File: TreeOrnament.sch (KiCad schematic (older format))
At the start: 13 parts, among them J1 USB_B_Micro

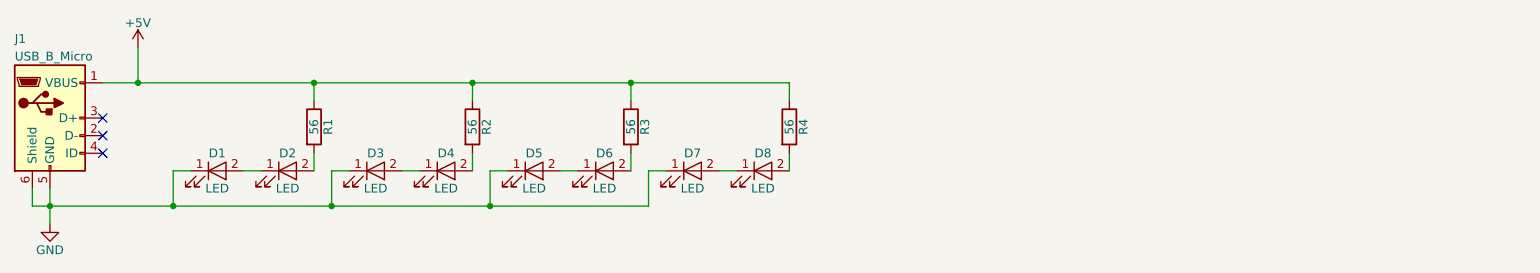
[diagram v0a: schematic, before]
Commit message: add more LEDs to schematic
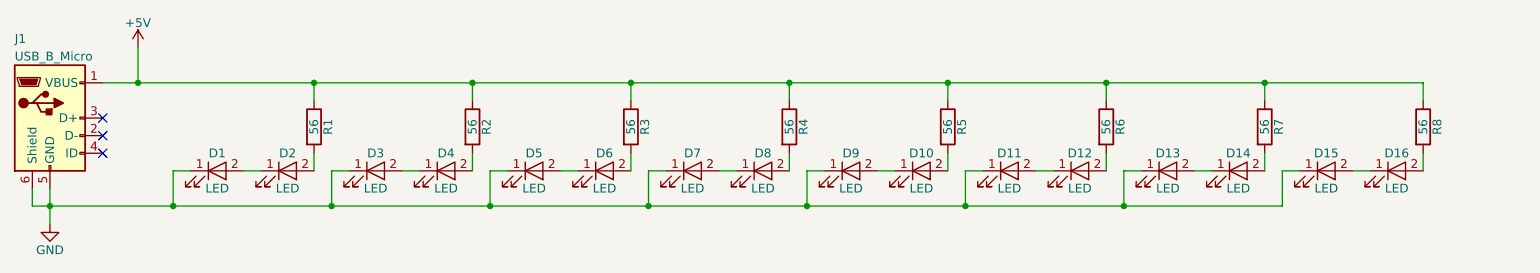
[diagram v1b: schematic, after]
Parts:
- added D10, D11, D12, D13, D14, D15, D16, D9: LED, LEDs:LED_D3.0mm, symbol LED
- added R5, R6, R7, R8: 56, Resistors_THT:R_Axial_DIN0207_L6.3mm_D2.5mm_P7.62mm_Horizontal, symbol R
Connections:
- net +5V: now also R5.1, R6.1, R7.1, R8.1
- net GND: now also D11.1 (K), D13.1 (K), D15.1 (K), D9.1 (K)
- new net: D10.1 (K), D9.2 (A)
- new net: D10.2 (A), R5.2
- new net: D11.2 (A), D12.1 (K)
- new net: D12.2 (A), R6.2
- new net: D13.2 (A), D14.1 (K)
- new net: D14.2 (A), R7.2
- new net: D15.2 (A), D16.1 (K)
- new net: D16.2 (A), R8.2
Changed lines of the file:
@@
 $EndComp
 Wire Wire Line
-	1800 1200 5700 1200
+	1800 1200 9300 1200
 Wire Wire Line
 	2000 1200 2000 1000
@@
 	1400 1800 1400 1900
 Wire Wire Line
-	1400 1900 4900 1900
+	1400 1900 8500 1900
 Connection ~ 1500 1900
 $Comp
@@
 NoConn ~ 1800 1500
 NoConn ~ 1800 1600
+$Comp
+L LED D9
+U 1 1 59F0E50C
+P 6050 1700
+F 0 "D9" H 6050 1800 50  0000 C CNN
+F 1 "LED" H 6050 1600 50  0000 C CNN
+F 2 "LEDs:LED_D3.0mm" H 6050 1700 50  0001 C CNN
+F 3 "" H 6050 1700 50  0001 C CNN
+	1    6050 1700
+	1    0    0    -1
+$EndComp
+$Comp
+L LED D10
+U 1 1 59F0ED31
+P 6450 1700
+F 0 "D10" H 6450 1800 50  0000 C CNN
+F 1 "LED" H 6450 1600 50  0000 C CNN
+F 2 "LEDs:LED_D3.0mm" H 6450 1700 50  0001 C CNN
+F 3 "" H 6450 1700 50  0001 C CNN
+	1    6450 1700
+	1    0    0    -1
+$EndComp
+$Comp
+L R R5
+U 1 1 59F0ED78
+P 6600 1450
+F 0 "R5" V 6680 1450 50  0000 C CNN
+F 1 "56" V 6600 1450 50  0000 C CNN
+F 2 "Resistors_THT:R_Axial_DIN0207_L6.3mm_D2.5mm_P7.62mm_Horizontal" V 6530 1450 50  0001 C CNN
+F 3 "" H 6600 1450 50  0001 C CNN
+	1    6600 1450
+	1    0    0    -1
+$EndComp
+Wire Wire Line
+	6600 1200 6600 1300
+Connection ~ 5700 1200
+Wire Wire Line
+	6600 1600 6600 1700
+Wire Wire Line
+	6300 1700 6200 1700
+Wire Wire Line
+	5900 1700 5800 1700
+Wire Wire Line
+	5800 1700 5800 1900
+Connection ~ 4900 1900
+$Comp
+L LED D11
+U 1 1 59F0EEA1
+P 6950 1700
+F 0 "D11" H 6950 1800 50  0000 C CNN
+F 1 "LED" H 6950 1600 50  0000 C CNN
+F 2 "LEDs:LED_D3.0mm" H 6950 1700 50  0001 C CNN
+F 3 "" H 6950 1700 50  0001 C CNN
+	1    6950 1700
+	1    0    0    -1
+$EndComp
+$Comp
+L LED D12
+U 1 1 59F0EEEE
+P 7350 1700
+F 0 "D12" H 7350 1800 50  0000 C CNN
+F 1 "LED" H 7350 1600 50  0000 C CNN
+F 2 "LEDs:LED_D3.0mm" H 7350 1700 50  0001 C CNN
+F 3 "" H 7350 1700 50  0001 C CNN
+	1    7350 1700
+	1    0    0    -1
+$EndComp
+$Comp
+L R R6
+U 1 1 59F0EF38
+P 7500 1450
+F 0 "R6" V 7580 1450 50  0000 C CNN
+F 1 "56" V 7500 1450 50  0000 C CNN
+F 2 "Resistors_THT:R_Axial_DIN0207_L6.3mm_D2.5mm_P7.62mm_Horizontal" V 7430 1450 50  0001 C CNN
+F 3 "" H 7500 1450 50  0001 C CNN
+	1    7500 1450
+	1    0    0    -1
+$EndComp
+Wire Wire Line
+	7500 1200 7500 1300
+Connection ~ 6600 1200
+Wire Wire Line
+	7500 1600 7500 1700
+Wire Wire Line
+	7200 1700 7100 1700
+Wire Wire Line
+	6800 1700 6700 1700
+Wire Wire Line
+	6700 1700 6700 1900
+Connection ~ 5800 1900
+$Comp
+L LED D13
+U 1 1 59F0F258
+P 7850 1700
+F 0 "D13" H 7850 1800 50  0000 C CNN
+F 1 "LED" H 7850 1600 50  0000 C CNN
+F 2 "LEDs:LED_D3.0mm" H 7850 1700 50  0001 C CNN
+F 3 "" H 7850 1700 50  0001 C CNN
+	1    7850 1700
+	1    0    0    -1
+$EndComp
+$Comp
+L LED D14
+U 1 1 59F0F2A9
+P 8250 1700
+F 0 "D14" H 8250 1800 50  0000 C CNN
+F 1 "LED" H 8250 1600 50  0000 C CNN
+F 2 "LEDs:LED_D3.0mm" H 8250 1700 50  0001 C CNN
+F 3 "" H 8250 1700 50  0001 C CNN
+	1    8250 1700
+	1    0    0    -1
+$EndComp
+$Comp
+L R R7
+U 1 1 59F0F2FD
+P 8400 1450
+F 0 "R7" V 8480 1450 50  0000 C CNN
+F 1 "56" V 8400 1450 50  0000 C CNN
+F 2 "Resistors_THT:R_Axial_DIN0207_L6.3mm_D2.5mm_P7.62mm_Horizontal" V 8330 1450 50  0001 C CNN
+F 3 "" H 8400 1450 50  0001 C CNN
+	1    8400 1450
+	1    0    0    -1
+$EndComp
+Wire Wire Line
+	8400 1200 8400 1300
+Connection ~ 7500 1200
+Wire Wire Line
+	8400 1600 8400 1700
+Wire Wire Line
+	8100 1700 8000 1700
+Wire Wire Line
+	7700 1700 7600 1700
+Wire Wire Line
+	7600 1700 7600 1900
+Connection ~ 6700 1900
+$Comp
+L LED D15
+U 1 1 59F0F481
+P 8750 1700
+F 0 "D15" H 8750 1800 50  0000 C CNN
+F 1 "LED" H 8750 1600 50  0000 C CNN
+F 2 "LEDs:LED_D3.0mm" H 8750 1700 50  0001 C CNN
+F 3 "" H 8750 1700 50  0001 C CNN
+	1    8750 1700
+	1    0    0    -1
+$EndComp
+$Comp
+L LED D16
+U 1 1 59F0F4DB
+P 9150 1700
+F 0 "D16" H 9150 1800 50  0000 C CNN
+F 1 "LED" H 9150 1600 50  0000 C CNN
+F 2 "LEDs:LED_D3.0mm" H 9150 1700 50  0001 C CNN
+F 3 "" H 9150 1700 50  0001 C CNN
+	1    9150 1700
+	1    0    0    -1
+$EndComp
+$Comp
+L R R8
+U 1 1 59F0F536
+P 9300 1450
+F 0 "R8" V 9380 1450 50  0000 C CNN
+F 1 "56" V 9300 1450 50  0000 C CNN
+F 2 "Resistors_THT:R_Axial_DIN0207_L6.3mm_D2.5mm_P7.62mm_Horizontal" V 9230 1450 50  0001 C CNN
+F 3 "" H 9300 1450 50  0001 C CNN
+	1    9300 1450
+	1    0    0    -1
+$EndComp
+Wire Wire Line
+	9300 1200 9300 1300
+Connection ~ 8400 1200
+Wire Wire Line
+	9300 1600 9300 1700
+Wire Wire Line
+	9000 1700 8900 1700
+Wire Wire Line
+	8600 1700 8500 1700
+Wire Wire Line
+	8500 1700 8500 1900
+Connection ~ 7600 1900
 $EndSCHEMATC

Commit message: remove extra resistor and LEDs
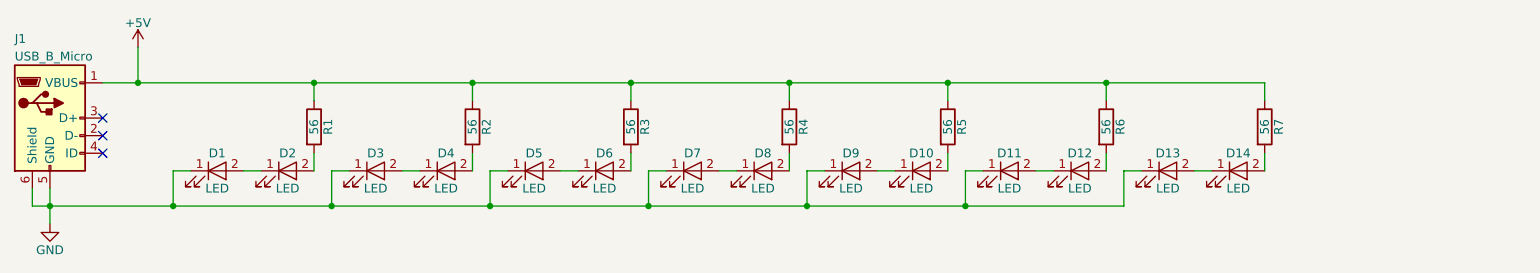
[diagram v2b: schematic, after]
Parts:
- removed D15, D16: LED, LEDs:LED_D3.0mm, symbol LED
- removed R8: 56, Resistors_THT:R_Axial_DIN0207_L6.3mm_D2.5mm_P7.62mm_Horizontal, symbol R
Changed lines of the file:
@@
 $EndComp
-Wire Wire Line
-	1800 1200 9300 1200
 Wire Wire Line
 	2000 1200 2000 1000
@@
 Wire Wire Line
 	1400 1800 1400 1900
-Wire Wire Line
-	1400 1900 8500 1900
 Connection ~ 1500 1900
 $Comp
@@
 	7600 1700 7600 1900
 Connection ~ 6700 1900
-$Comp
-L LED D15
-U 1 1 59F0F481
-P 8750 1700
-F 0 "D15" H 8750 1800 50  0000 C CNN
-F 1 "LED" H 8750 1600 50  0000 C CNN
-F 2 "LEDs:LED_D3.0mm" H 8750 1700 50  0001 C CNN
-F 3 "" H 8750 1700 50  0001 C CNN
-	1    8750 1700
-	1    0    0    -1
-$EndComp
-$Comp
-L LED D16
-U 1 1 59F0F4DB
-P 9150 1700
-F 0 "D16" H 9150 1800 50  0000 C CNN
-F 1 "LED" H 9150 1600 50  0000 C CNN
-F 2 "LEDs:LED_D3.0mm" H 9150 1700 50  0001 C CNN
-F 3 "" H 9150 1700 50  0001 C CNN
-	1    9150 1700
-	1    0    0    -1
-$EndComp
-$Comp
-L R R8
-U 1 1 59F0F536
-P 9300 1450
-F 0 "R8" V 9380 1450 50  0000 C CNN
-F 1 "56" V 9300 1450 50  0000 C CNN
-F 2 "Resistors_THT:R_Axial_DIN0207_L6.3mm_D2.5mm_P7.62mm_Horizontal" V 9230 1450 50  0001 C CNN
-F 3 "" H 9300 1450 50  0001 C CNN
-	1    9300 1450
-	1    0    0    -1
-$EndComp
-Wire Wire Line
-	9300 1200 9300 1300
-Connection ~ 8400 1200
-Wire Wire Line
-	9300 1600 9300 1700
-Wire Wire Line
-	9000 1700 8900 1700
-Wire Wire Line
-	8600 1700 8500 1700
-Wire Wire Line
-	8500 1700 8500 1900
-Connection ~ 7600 1900
+Wire Wire Line
+	7600 1900 1400 1900
+Wire Wire Line
+	1800 1200 8400 1200
 $EndSCHEMATC

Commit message: use silkless footprints
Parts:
- D1, D10, D11, D12, D13, D14, D2, D3, D4, D5, D6, D7, D8, D9: footprint LEDs:LED_D3.0mm -> myLibrary:LED_D3.0mm
- R1, R2, R3, R4, R5, R6, R7: footprint Resistors_THT:R_Axial_DIN0207_L6.3mm_D2.5mm_P7.62mm_Horizontal -> myLibrary:R_Axial_DIN0207_L6.3mm_D2.5mm_P7.62mm_Horizontal
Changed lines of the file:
@@
 F 0 "R1" V 3080 1450 50  0000 C CNN
 F 1 "56" V 3000 1450 50  0000 C CNN
-F 2 "Resistors_THT:R_Axial_DIN0207_L6.3mm_D2.5mm_P7.62mm_Horizontal" V 2930 1450 50  0001 C CNN
+F 2 "myLibrary:R_Axial_DIN0207_L6.3mm_D2.5mm_P7.62mm_Horizontal" V 2930 1450 50  0001 C CNN
 F 3 "" H 3000 1450 50  0001 C CNN
 	1    3000 1450
@@
 F 0 "D1" H 2450 1800 50  0000 C CNN
 F 1 "LED" H 2450 1600 50  0000 C CNN
-F 2 "LEDs:LED_D3.0mm" H 2450 1700 50  0001 C CNN
+F 2 "myLibrary:LED_D3.0mm" H 2450 1700 50  0001 C CNN
 F 3 "" H 2450 1700 50  0001 C CNN
 	1    2450 1700
@@
 F 0 "D2" H 2850 1800 50  0000 C CNN
 F 1 "LED" H 2850 1600 50  0000 C CNN
-F 2 "LEDs:LED_D3.0mm" H 2850 1700 50  0001 C CNN
+F 2 "myLibrary:LED_D3.0mm" H 2850 1700 50  0001 C CNN
 F 3 "" H 2850 1700 50  0001 C CNN
 	1    2850 1700
@@
 F 0 "R2" V 3980 1450 50  0000 C CNN
 F 1 "56" V 3900 1450 50  0000 C CNN
-F 2 "Resistors_THT:R_Axial_DIN0207_L6.3mm_D2.5mm_P7.62mm_Horizontal" V 3830 1450 50  0001 C CNN
+F 2 "myLibrary:R_Axial_DIN0207_L6.3mm_D2.5mm_P7.62mm_Horizontal" V 3830 1450 50  0001 C CNN
 F 3 "" H 3900 1450 50  0001 C CNN
 	1    3900 1450
@@
 F 0 "D3" H 3350 1800 50  0000 C CNN
 F 1 "LED" H 3350 1600 50  0000 C CNN
-F 2 "LEDs:LED_D3.0mm" H 3350 1700 50  0001 C CNN
+F 2 "myLibrary:LED_D3.0mm" H 3350 1700 50  0001 C CNN
 F 3 "" H 3350 1700 50  0001 C CNN
 	1    3350 1700
@@
 F 0 "D4" H 3750 1800 50  0000 C CNN
 F 1 "LED" H 3750 1600 50  0000 C CNN
-F 2 "LEDs:LED_D3.0mm" H 3750 1700 50  0001 C CNN
+F 2 "myLibrary:LED_D3.0mm" H 3750 1700 50  0001 C CNN
 F 3 "" H 3750 1700 50  0001 C CNN
 	1    3750 1700
@@
 F 0 "D5" H 4250 1800 50  0000 C CNN
 F 1 "LED" H 4250 1600 50  0000 C CNN
-F 2 "LEDs:LED_D3.0mm" H 4250 1700 50  0001 C CNN
+F 2 "myLibrary:LED_D3.0mm" H 4250 1700 50  0001 C CNN
 F 3 "" H 4250 1700 50  0001 C CNN
 	1    4250 1700
@@
 F 0 "D6" H 4650 1800 50  0000 C CNN
 F 1 "LED" H 4650 1600 50  0000 C CNN
-F 2 "LEDs:LED_D3.0mm" H 4650 1700 50  0001 C CNN
+F 2 "myLibrary:LED_D3.0mm" H 4650 1700 50  0001 C CNN
 F 3 "" H 4650 1700 50  0001 C CNN
 	1    4650 1700
@@
 F 0 "R3" V 4880 1450 50  0000 C CNN
 F 1 "56" V 4800 1450 50  0000 C CNN
-F 2 "Resistors_THT:R_Axial_DIN0207_L6.3mm_D2.5mm_P7.62mm_Horizontal" V 4730 1450 50  0001 C CNN
+F 2 "myLibrary:R_Axial_DIN0207_L6.3mm_D2.5mm_P7.62mm_Horizontal" V 4730 1450 50  0001 C CNN
 F 3 "" H 4800 1450 50  0001 C CNN
 	1    4800 1450
@@
 F 0 "D7" H 5150 1800 50  0000 C CNN
 F 1 "LED" H 5150 1600 50  0000 C CNN
-F 2 "LEDs:LED_D3.0mm" H 5150 1700 50  0001 C CNN
+F 2 "myLibrary:LED_D3.0mm" H 5150 1700 50  0001 C CNN
 F 3 "" H 5150 1700 50  0001 C CNN
 	1    5150 1700
@@
 F 0 "D8" H 5550 1800 50  0000 C CNN
 F 1 "LED" H 5550 1600 50  0000 C CNN
-F 2 "LEDs:LED_D3.0mm" H 5550 1700 50  0001 C CNN
+F 2 "myLibrary:LED_D3.0mm" H 5550 1700 50  0001 C CNN
 F 3 "" H 5550 1700 50  0001 C CNN
 	1    5550 1700
@@
 F 0 "R4" V 5780 1450 50  0000 C CNN
 F 1 "56" V 5700 1450 50  0000 C CNN
-F 2 "Resistors_THT:R_Axial_DIN0207_L6.3mm_D2.5mm_P7.62mm_Horizontal" V 5630 1450 50  0001 C CNN
+F 2 "myLibrary:R_Axial_DIN0207_L6.3mm_D2.5mm_P7.62mm_Horizontal" V 5630 1450 50  0001 C CNN
 F 3 "" H 5700 1450 50  0001 C CNN
 	1    5700 1450
@@
 F 0 "D9" H 6050 1800 50  0000 C CNN
 F 1 "LED" H 6050 1600 50  0000 C CNN
-F 2 "LEDs:LED_D3.0mm" H 6050 1700 50  0001 C CNN
+F 2 "myLibrary:LED_D3.0mm" H 6050 1700 50  0001 C CNN
 F 3 "" H 6050 1700 50  0001 C CNN
 	1    6050 1700
@@
 F 0 "D10" H 6450 1800 50  0000 C CNN
 F 1 "LED" H 6450 1600 50  0000 C CNN
-F 2 "LEDs:LED_D3.0mm" H 6450 1700 50  0001 C CNN
+F 2 "myLibrary:LED_D3.0mm" H 6450 1700 50  0001 C CNN
 F 3 "" H 6450 1700 50  0001 C CNN
 	1    6450 1700
@@
 F 0 "R5" V 6680 1450 50  0000 C CNN
 F 1 "56" V 6600 1450 50  0000 C CNN
-F 2 "Resistors_THT:R_Axial_DIN0207_L6.3mm_D2.5mm_P7.62mm_Horizontal" V 6530 1450 50  0001 C CNN
+F 2 "myLibrary:R_Axial_DIN0207_L6.3mm_D2.5mm_P7.62mm_Horizontal" V 6530 1450 50  0001 C CNN
 F 3 "" H 6600 1450 50  0001 C CNN
 	1    6600 1450
@@
 F 0 "D11" H 6950 1800 50  0000 C CNN
 F 1 "LED" H 6950 1600 50  0000 C CNN
-F 2 "LEDs:LED_D3.0mm" H 6950 1700 50  0001 C CNN
+F 2 "myLibrary:LED_D3.0mm" H 6950 1700 50  0001 C CNN
 F 3 "" H 6950 1700 50  0001 C CNN
 	1    6950 1700
@@
 F 0 "D12" H 7350 1800 50  0000 C CNN
 F 1 "LED" H 7350 1600 50  0000 C CNN
-F 2 "LEDs:LED_D3.0mm" H 7350 1700 50  0001 C CNN
+F 2 "myLibrary:LED_D3.0mm" H 7350 1700 50  0001 C CNN
 F 3 "" H 7350 1700 50  0001 C CNN
 	1    7350 1700
@@
 F 0 "R6" V 7580 1450 50  0000 C CNN
 F 1 "56" V 7500 1450 50  0000 C CNN
-F 2 "Resistors_THT:R_Axial_DIN0207_L6.3mm_D2.5mm_P7.62mm_Horizontal" V 7430 1450 50  0001 C CNN
+F 2 "myLibrary:R_Axial_DIN0207_L6.3mm_D2.5mm_P7.62mm_Horizontal" V 7430 1450 50  0001 C CNN
 F 3 "" H 7500 1450 50  0001 C CNN
 	1    7500 1450
@@
 F 0 "D13" H 7850 1800 50  0000 C CNN
 F 1 "LED" H 7850 1600 50  0000 C CNN
-F 2 "LEDs:LED_D3.0mm" H 7850 1700 50  0001 C CNN
+F 2 "myLibrary:LED_D3.0mm" H 7850 1700 50  0001 C CNN
 F 3 "" H 7850 1700 50  0001 C CNN
 	1    7850 1700
@@
 F 0 "D14" H 8250 1800 50  0000 C CNN
 F 1 "LED" H 8250 1600 50  0000 C CNN
-F 2 "LEDs:LED_D3.0mm" H 8250 1700 50  0001 C CNN
+F 2 "myLibrary:LED_D3.0mm" H 8250 1700 50  0001 C CNN
 F 3 "" H 8250 1700 50  0001 C CNN
 	1    8250 1700
@@
 F 0 "R7" V 8480 1450 50  0000 C CNN
 F 1 "56" V 8400 1450 50  0000 C CNN
-F 2 "Resistors_THT:R_Axial_DIN0207_L6.3mm_D2.5mm_P7.62mm_Horizontal" V 8330 1450 50  0001 C CNN
+F 2 "myLibrary:R_Axial_DIN0207_L6.3mm_D2.5mm_P7.62mm_Horizontal" V 8330 1450 50  0001 C CNN
 F 3 "" H 8400 1450 50  0001 C CNN
 	1    8400 1450
